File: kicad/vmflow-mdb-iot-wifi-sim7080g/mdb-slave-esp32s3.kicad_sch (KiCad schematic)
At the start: 40 parts, among them J1 MDB_Connector, J2 USB_C_Receptacle_USB2.0_16P, J3 Conn_02x11_Odd_Even, J4 JAE_SIM_Card_SF72S006, SW1 SW_Push, U1 TLP785, U2 SIM7080G, U3 ESP32-S3FH4R2, U4 TLP785, U5 LM2594HVM-3.3, Y1 Crystal_GND24

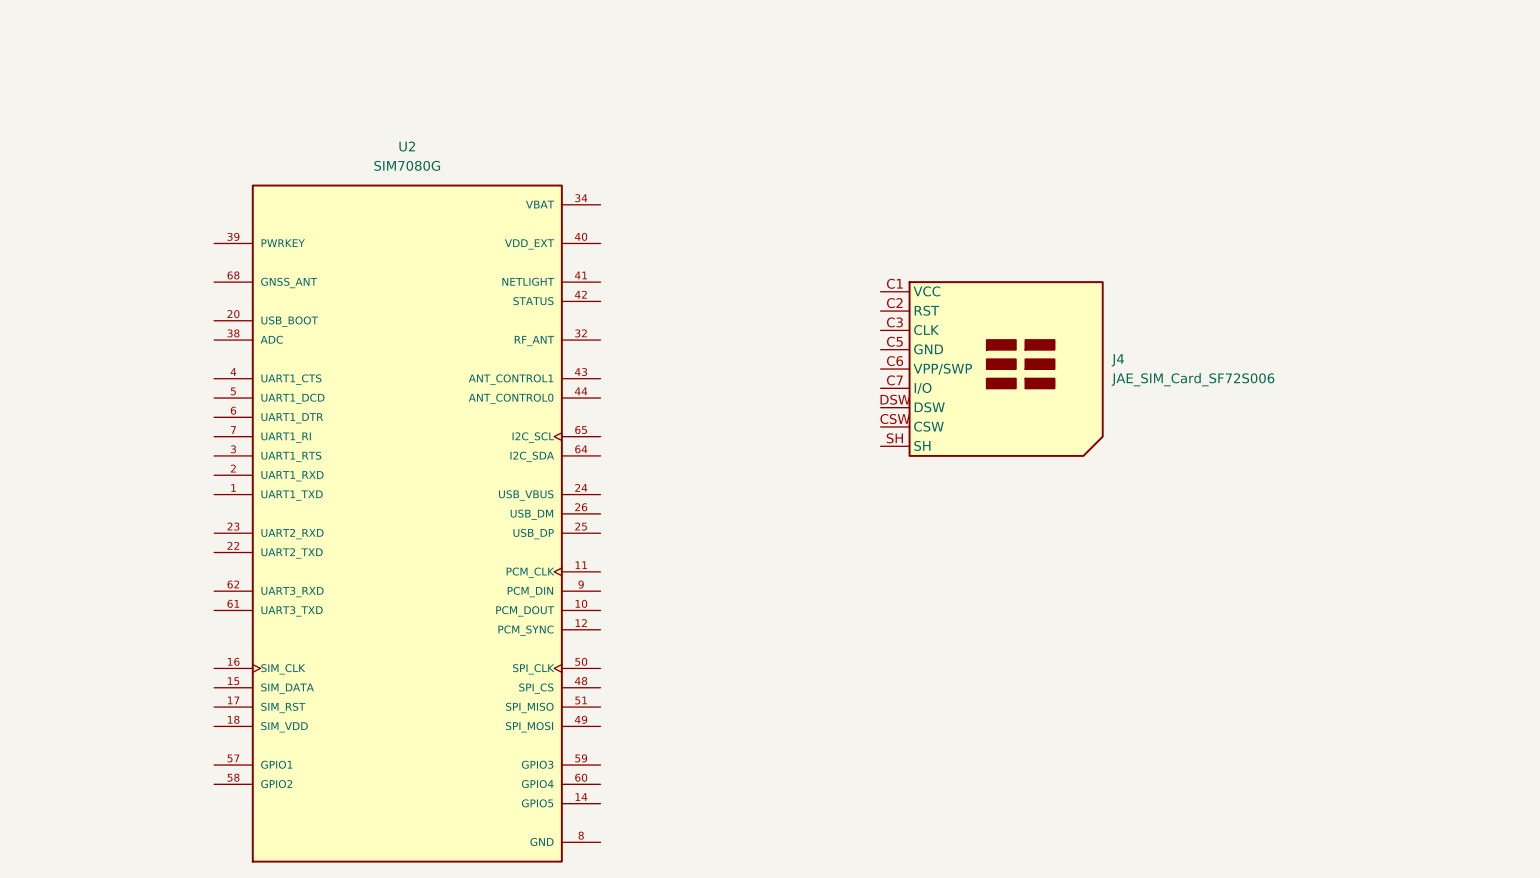
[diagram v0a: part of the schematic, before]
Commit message: Connecting sim7080G to simcard
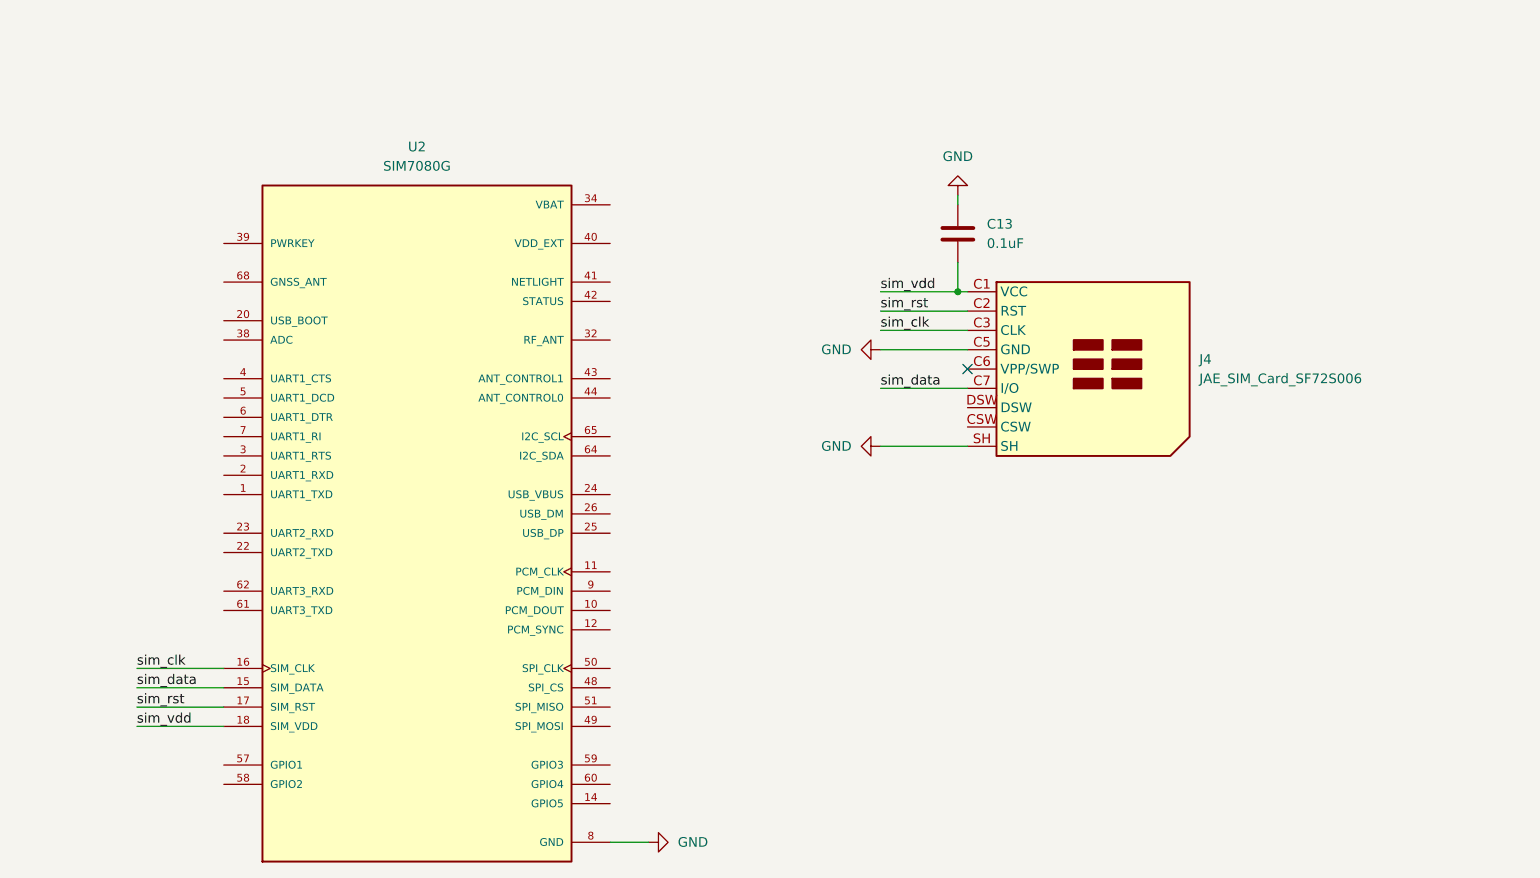
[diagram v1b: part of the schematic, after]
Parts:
- added C13: 0.1uF, Capacitor_SMD:C_0603_1608Metric, symbol Device:C
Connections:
- net GND: now also J4.C5 (GND), J4.SH, C13.2
- net sim_vdd: now reaches J4.C1 (VCC)
- net sim_vdd: now also U2.18 (SIM_VDD), C13.1
- net sim_rst: now reaches J4.C2 (RST)
- net sim_rst: now also U2.17 (SIM_RST)
- net sim_clk: now reaches J4.C3 (CLK)
- net sim_clk: now also U2.16 (SIM_CLK)
- net sim_data: now reaches J4.C7 (I/O)
- net sim_data: now also U2.15 (SIM_DATA)
- no-connect marks 30 -> 31
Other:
- moved on the sheet: J4, U2
